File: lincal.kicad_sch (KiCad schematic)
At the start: 0 parts

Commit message: More work in progres
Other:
- added sheet Reference (ref.kicad_sch)
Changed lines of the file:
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@@
 	(paper "A4")
+	(sheet
+		(at 54.61 96.52)
+		(size 38.1 22.86)
+		(exclude_from_sim no)
+		(in_bom yes)
+		(on_board yes)
+		(dnp no)
+		(fields_autoplaced yes)
+		(stroke
+			(width 0.1524)
+			(type solid)
+		)
+		(fill
+			(color 0 0 0 0.0000)
+		)
+		(property "Sheetname" "Reference"
+			(at 54.61 95.8084 0)
+			(effects
+				(font
+					(size 1.27 1.27)
+				)
+				(justify left bottom)
+			)
+		)
+		(property "Sheetfile" "ref.kicad_sch"
+			(at 54.61 119.9646 0)
+			(effects
+				(font
+					(size 1.27 1.27)
+				)
+				(justify left top)
+			)
+		)
+		(instances
+			(project "lincal"
+				(path "/b054cef4-39e3-49d8-aff0-7ba5a206c187"
+					(page "9")
+				)
+			)
+		)
+	)
 	(sheet
 		(at 176.53 53.34)
@@
 			(project "lincal"
 				(path "/b054cef4-39e3-49d8-aff0-7ba5a206c187"
-					(page "4")
+					(page "2b")
 				)
 			)
@@
 			(project "lincal"
 				(path "/b054cef4-39e3-49d8-aff0-7ba5a206c187"
-					(page "8")
+					(page "5a")
 				)
 			)
@@
 			(project "lincal"
 				(path "/b054cef4-39e3-49d8-aff0-7ba5a206c187"
-					(page "3")
+					(page "2a")
 				)
 			)
@@
 			(project "lincal"
 				(path "/b054cef4-39e3-49d8-aff0-7ba5a206c187"
-					(page "7")
+					(page "4a")
 				)
 			)
@@
 			(project "lincal"
 				(path "/b054cef4-39e3-49d8-aff0-7ba5a206c187"
-					(page "6")
+					(page "3a")
 				)
 			)
@@
 			(project "lincal"
 				(path "/b054cef4-39e3-49d8-aff0-7ba5a206c187"
-					(page "2")
+					(page "1a")
 				)
 			)
@@
 	(sheet_instances
 		(path "/"
-			(page "1")
-		)
-	)
+			(page "0")
+		)
+	)

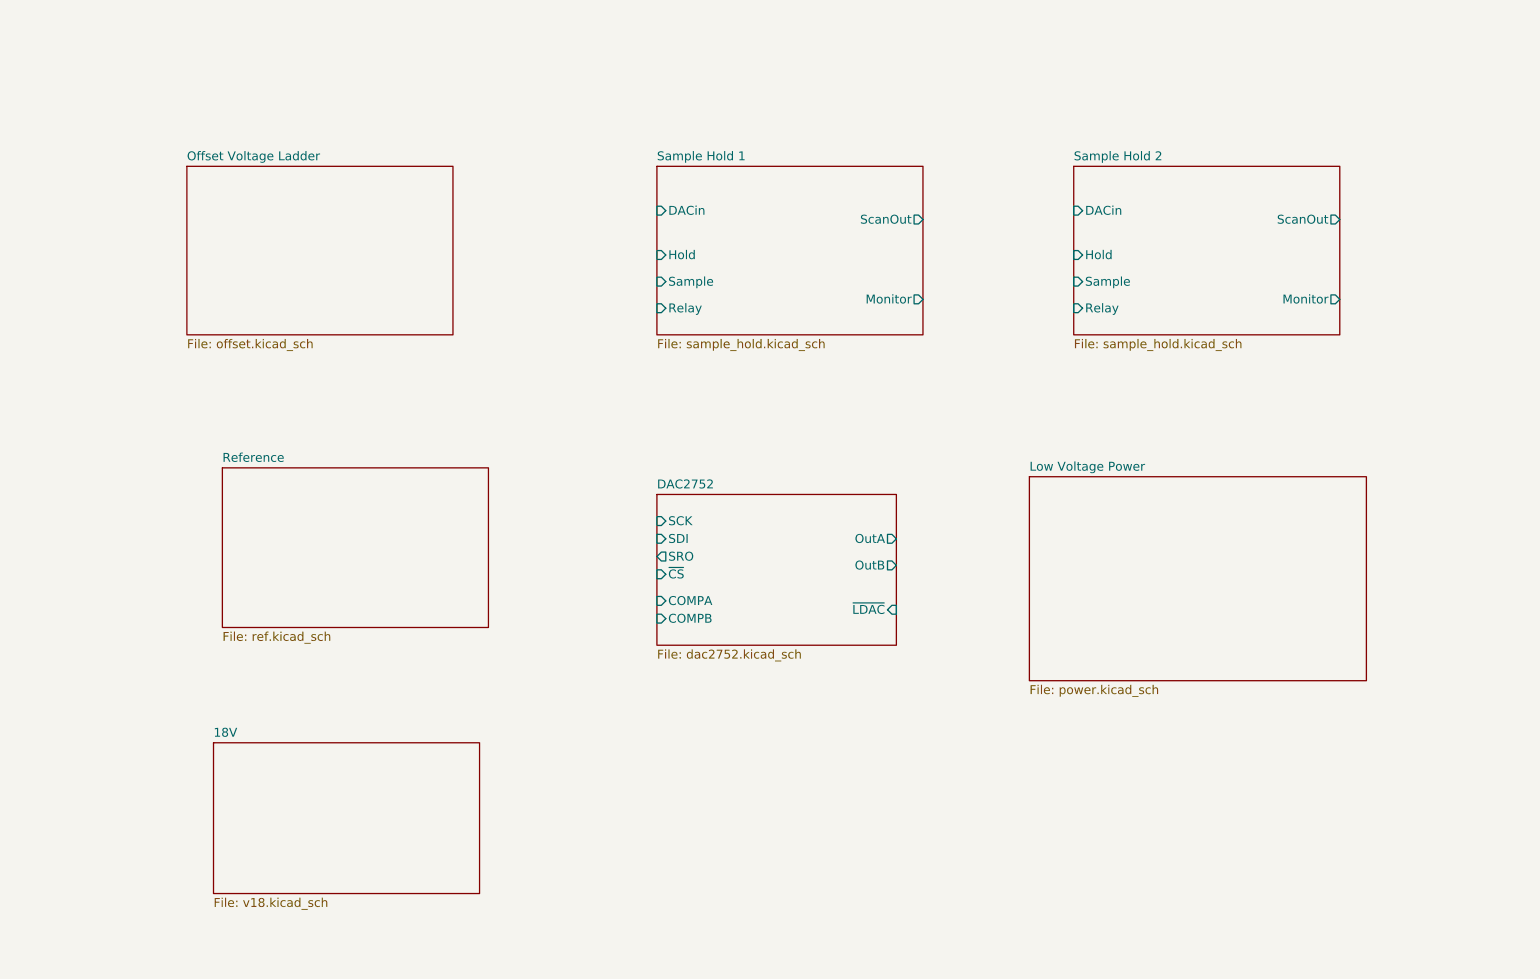
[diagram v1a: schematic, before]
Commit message: Analog side is more or less complete.
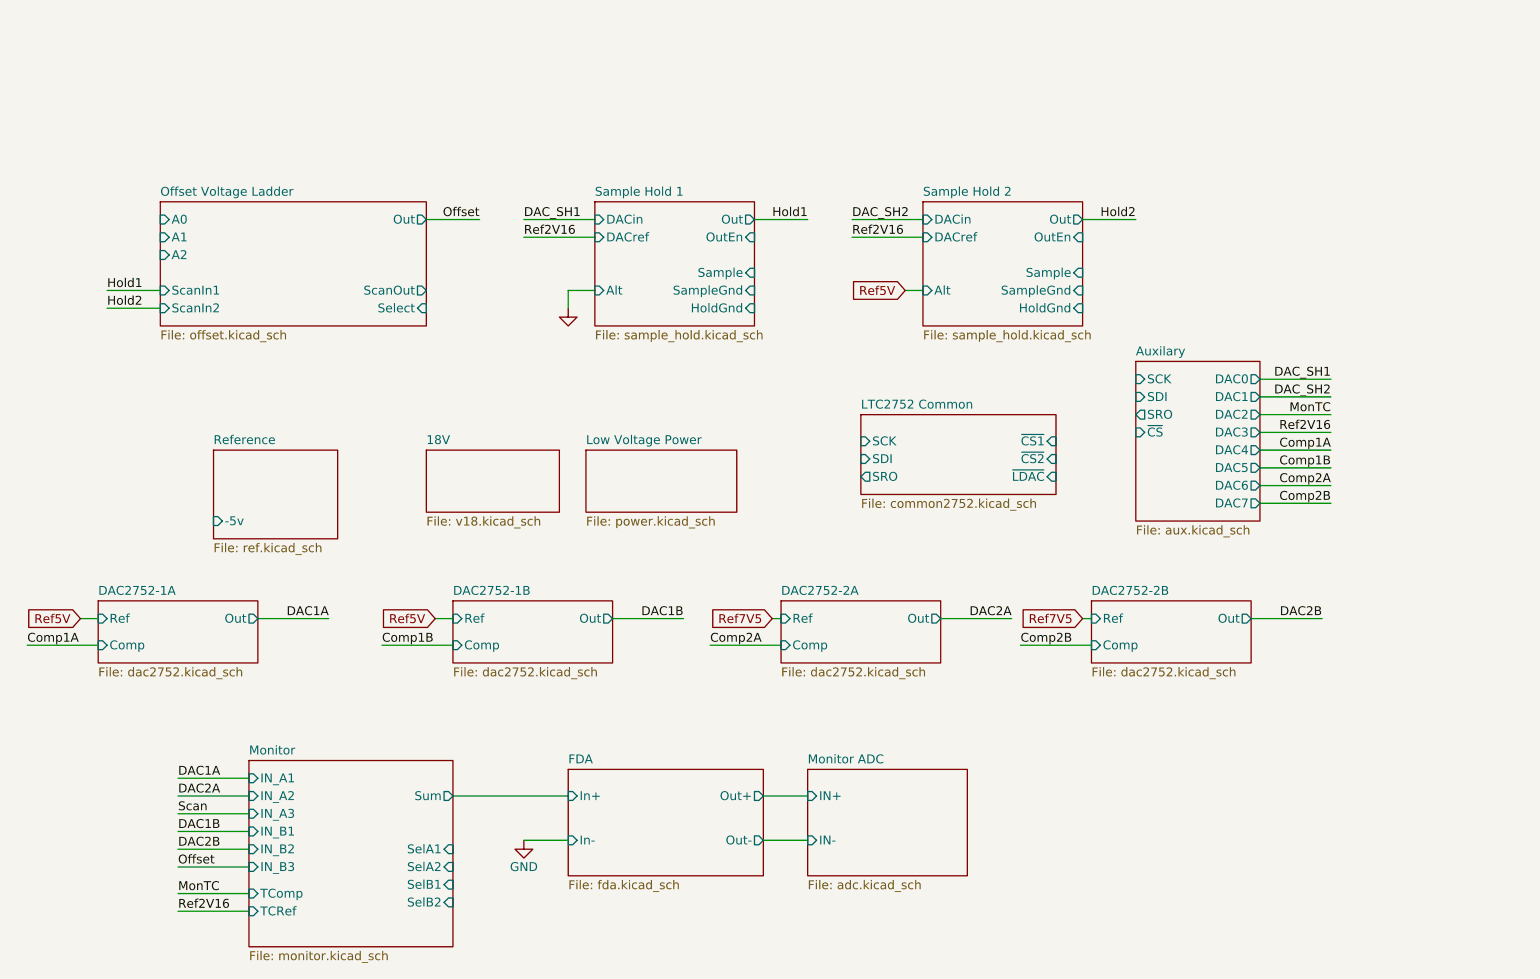
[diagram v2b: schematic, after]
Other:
- sheet DAC2752 renamed DAC2752-1A
- added sheet Auxilary (aux.kicad_sch)
- added sheet DAC2752-1B (dac2752.kicad_sch)
- added sheet DAC2752-2A (dac2752.kicad_sch)
- added sheet DAC2752-2B (dac2752.kicad_sch)
- added sheet FDA (fda.kicad_sch)
- added sheet LTC2752 Common (common2752.kicad_sch)
- added sheet Monitor (monitor.kicad_sch)
- added sheet Monitor ADC (adc.kicad_sch)
- sheet DAC2752-1A ports: added Comp, Out, Ref; removed COMPA, COMPB, OutA, OutB, SCK, SDI, SRO, ~{CS}, ~{LDAC}
- sheet Offset Voltage Ladder ports: added A0, A1, A2, Out, ScanIn1, ScanIn2, ScanOut, Select; removed none
- sheet Reference ports: added -5v; removed none
- sheet Sample Hold 1 ports: added Alt, DACref, HoldGnd, Out, OutEn, SampleGnd; removed Hold, Monitor, Relay, ScanOut
- sheet Sample Hold 2 ports: added Alt, DACref, HoldGnd, Out, OutEn, SampleGnd; removed Hold, Monitor, Relay, ScanOut

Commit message: Little simplifications etc.
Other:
- added sheet CPU (cpu.kicad_sch)
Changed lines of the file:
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@@
+	)
+	(sheet
+		(at 179.07 138.43)
+		(size 22.86 16.51)
+		(exclude_from_sim no)
+		(in_bom yes)
+		(on_board yes)
+		(dnp no)
+		(fields_autoplaced yes)
+		(stroke
+			(width 0.1524)
+			(type solid)
+		)
+		(fill
+			(color 0 0 0 0.0000)
+		)
+		(property "Sheetname" "CPU"
+			(at 179.07 137.7184 0)
+			(effects
+				(font
+					(size 1.27 1.27)
+				)
+				(justify left bottom)
+			)
+		)
+		(property "Sheetfile" "cpu.kicad_sch"
+			(at 179.07 155.5246 0)
+			(effects
+				(font
+					(size 1.27 1.27)
+				)
+				(justify left top)
+			)
+		)
+		(instances
+			(project "lincal"
+				(path "/b054cef4-39e3-49d8-aff0-7ba5a206c187"
+					(page "9a")
+				)
+			)
+		)
 	)
 	(sheet

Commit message: Schematic complete, maybe
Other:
- sheet CPU ports: added MISO, MOSI, MonA0, MonA1, MonB0, MonB1, OffsetA0, OffsetA1, OffsetA2, SCK, SHHoldG1, SHHoldG2, SHOutEn1, SHOutEn2, SHSample1, SHSample2, SHSampleG1, SHSampleG2, SHSel, ~{CS2}, ~{CS3}, ~{CS4}, ~{CS5}, ~{LDAC}; removed none
- sheet FDA ports: added IN+, IN-; removed In+, In-
- sheet Monitor ports: added SelA0, SelB0; removed SelA2, SelB2
- sheet Monitor ADC ports: added DIN, DOUT, SCLK, ~{CS}; removed none
- sheet Reference ports: added none; removed -5v

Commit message: Everything assigned except for wierd shit.
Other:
- sheet CPU ports: added Sel1A, Sel1B, Sel2A, Sel2B; removed none
- sheet DAC2752-1A ports: added Select; removed none
- sheet DAC2752-1B ports: added Select; removed none
- sheet DAC2752-2A ports: added Select; removed none
- sheet DAC2752-2B ports: added Select; removed none

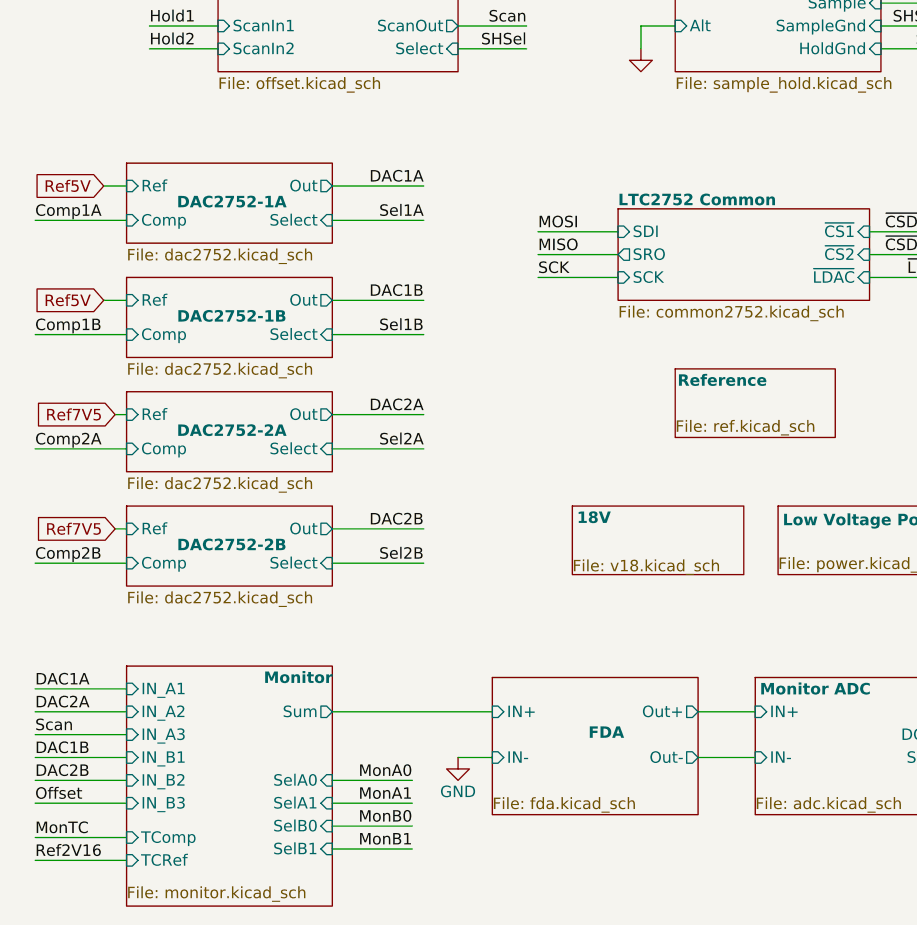
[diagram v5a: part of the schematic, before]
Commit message: Tweaks following spice simulation.
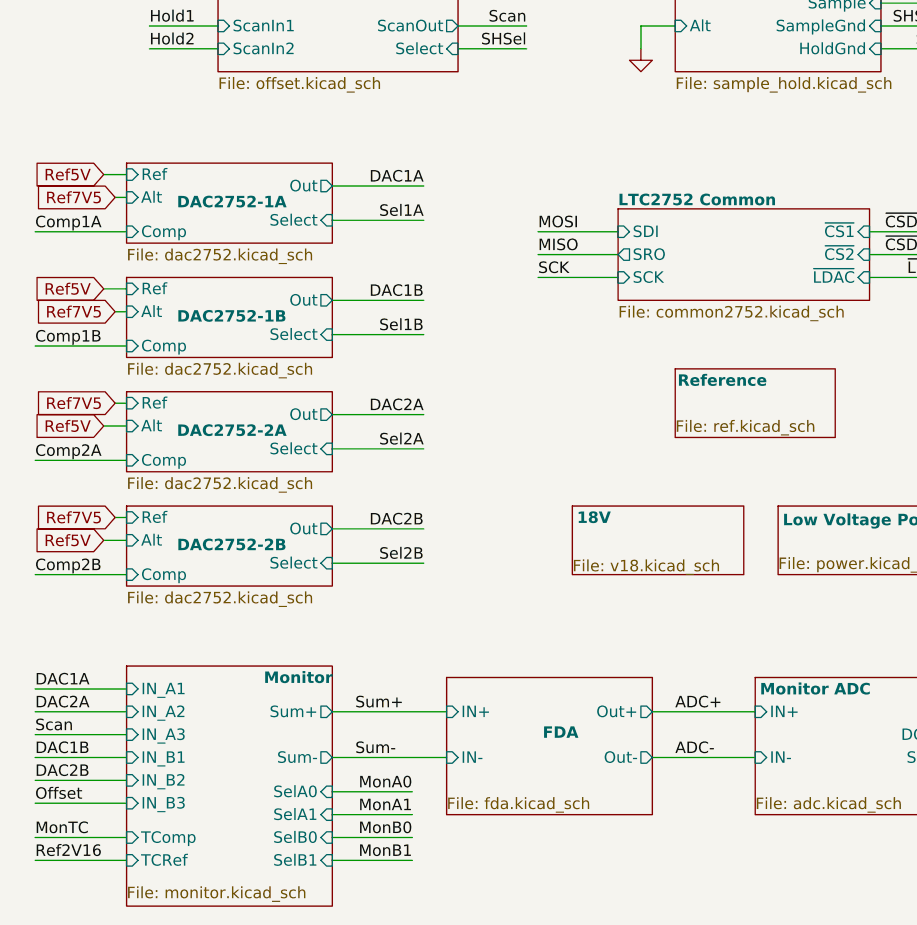
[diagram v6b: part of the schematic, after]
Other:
- sheet DAC2752-1A ports: added Alt; removed none
- sheet DAC2752-1B ports: added Alt; removed none
- sheet DAC2752-2A ports: added Alt; removed none
- sheet DAC2752-2B ports: added Alt; removed none
- sheet Monitor ports: added Sum+, Sum-; removed Sum

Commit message: Scan deleted.
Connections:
- no-connect marks 0 -> 2
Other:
- removed sheet Sample Hold 1
- removed sheet Sample Hold 2
- sheet CPU ports: added none; removed SHHoldG1, SHHoldG2, SHOutEn1, SHOutEn2, SHSample1, SHSample2, SHSampleG1, SHSampleG2
